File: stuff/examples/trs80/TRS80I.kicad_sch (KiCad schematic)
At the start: 73 parts, among them U1 4011, U6 4023

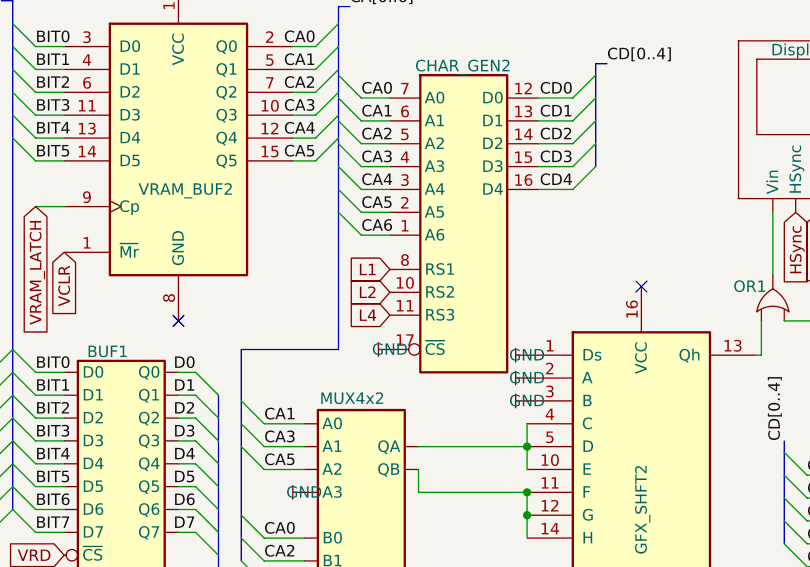
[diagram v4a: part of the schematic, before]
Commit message: MCM6670 map fix
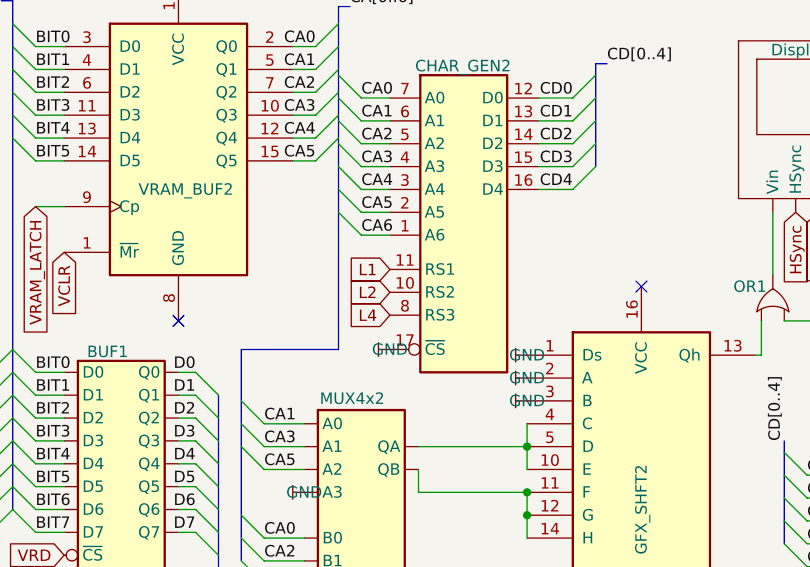
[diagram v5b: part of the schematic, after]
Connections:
- net L1: now also CHAR_GEN2.11 (RS1); no longer CHAR_GEN2.8 (RS1)
- net L4: now also CHAR_GEN2.8 (RS3); no longer CHAR_GEN2.11 (RS3)
